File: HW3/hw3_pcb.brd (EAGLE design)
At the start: 50 x 50 mm, 22 parts, among them J1 USB-MB-H, U1 PIC32MX250F128B, U2 SLIDE, U3 MCP1702, U5 USER, U9 8MHz

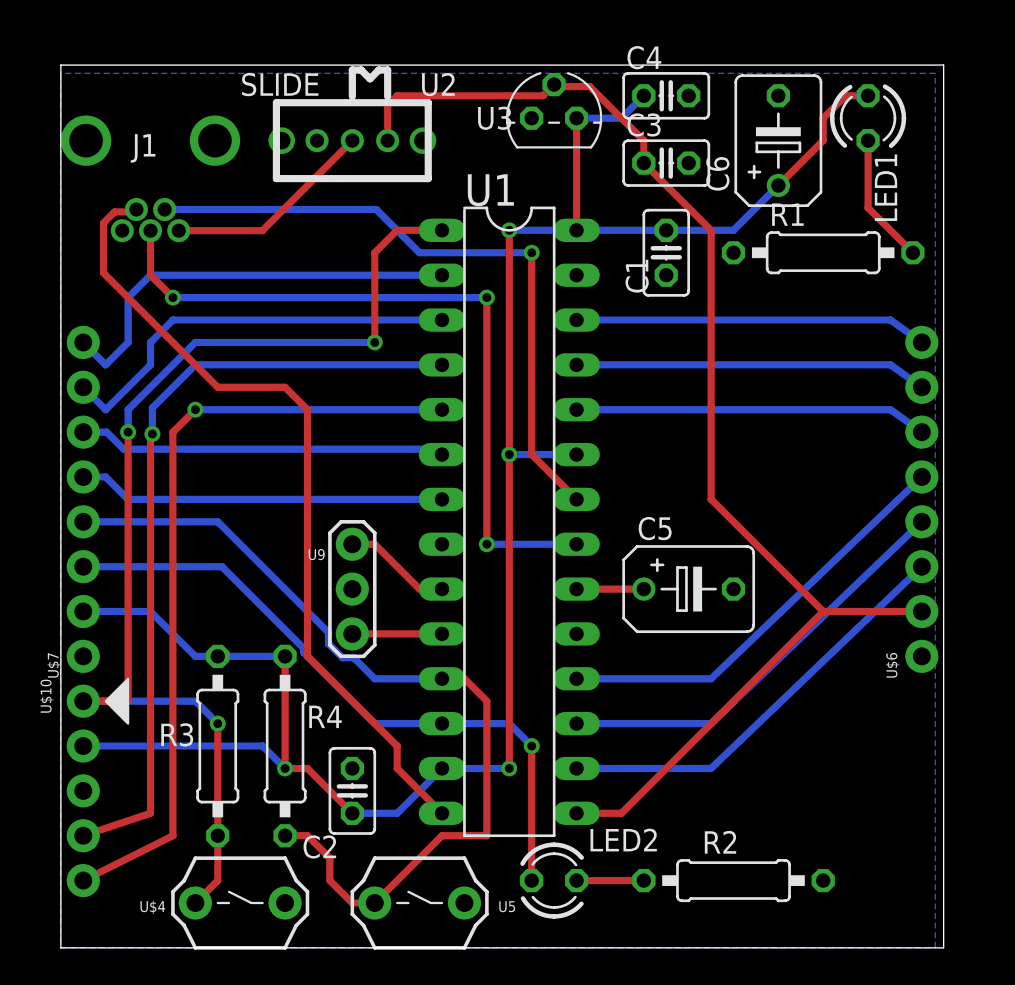
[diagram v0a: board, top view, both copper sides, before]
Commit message: Error checking complete. PCD complete. Had to modify USB pin spacing so I updated the library and schematic accordingly
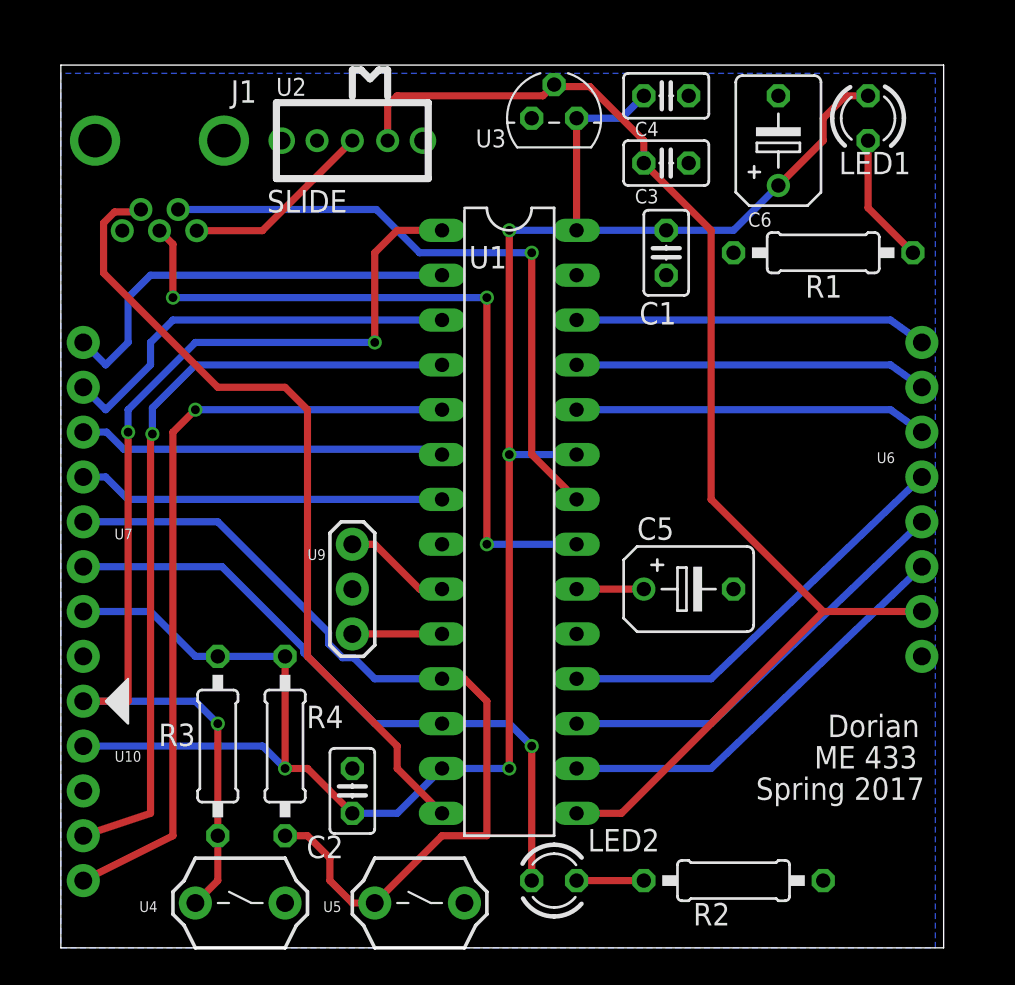
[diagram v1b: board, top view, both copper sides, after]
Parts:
- moved J1 0.51 mm to (5.59, 45.7)
- renumbered U$10 to U10, U$4 to U4, U$6 to U6, U$7 to U7
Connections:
- net N$5 renamed OSC1/A2
- net N$6 renamed OSC2/A3
- net N$8 renamed VCAP
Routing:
- net N$1: track 11.9 -> 10.9 mm
- net D-: track 36.8 -> 36.1 mm
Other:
- board text added: "Dorian"
- board text added: "ME 433"
- board text added: "Spring 2017"
